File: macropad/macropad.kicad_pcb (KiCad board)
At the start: 2 copper layers, 77.5 x 61 mm, 45 parts, among them IC1 W25Q16JVUXIQ_TR, J1 Conn_01x03_Female, J2 USB_C_Receptacle, SW1 BOOT, SW2 RESET, U1 RP2040, U10 DRV5057A3, U11 DRV5057A3, U12 OLED_256x64_I2C, U2 DRV5057A3, U3 DRV5057A3, U4 DRV5057A3, U5 DRV5057A3, U6 CD74HC4067SM96E4, U7 DRV5057A3, U8 DRV5057A3, U9 NCP1117-3.3_SOT223, Y1 ABLS-12.000MHZ-B4-T

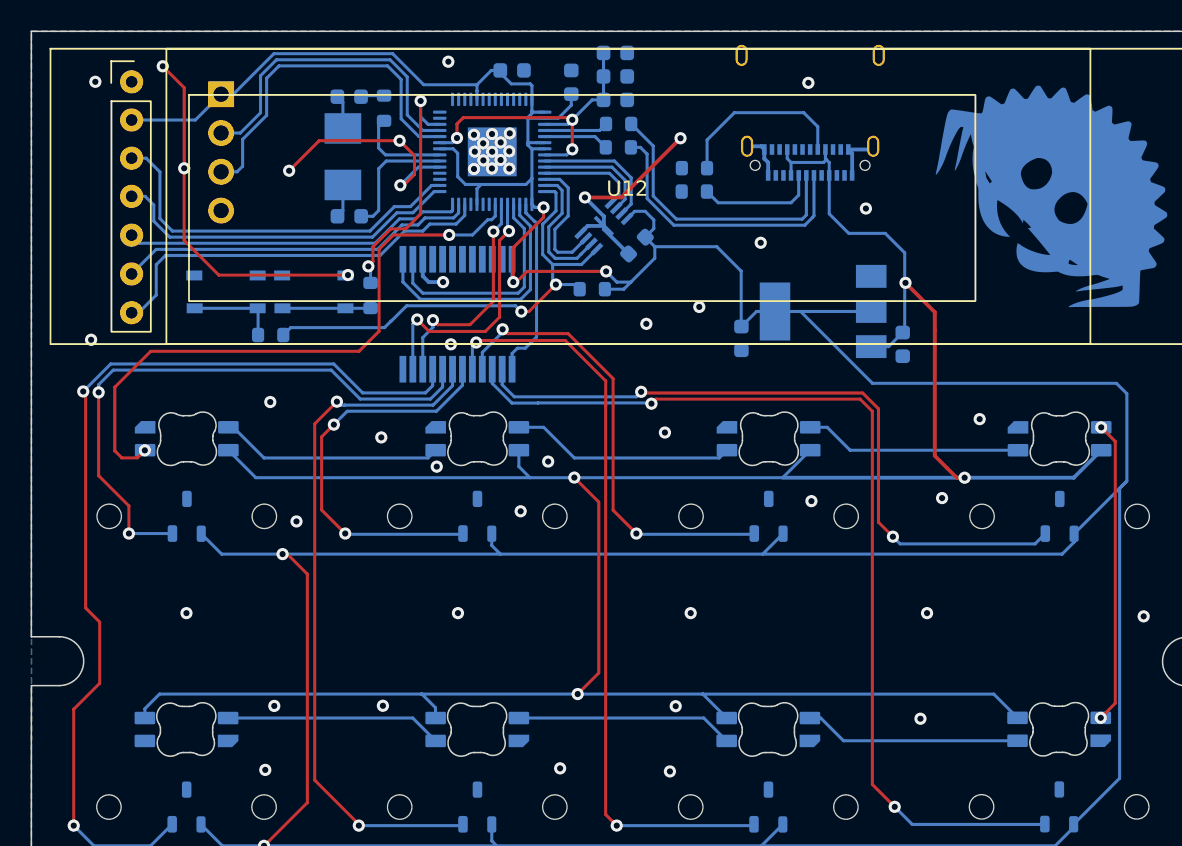
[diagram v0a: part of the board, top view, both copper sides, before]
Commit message: fix multiple issues with macropad pcb
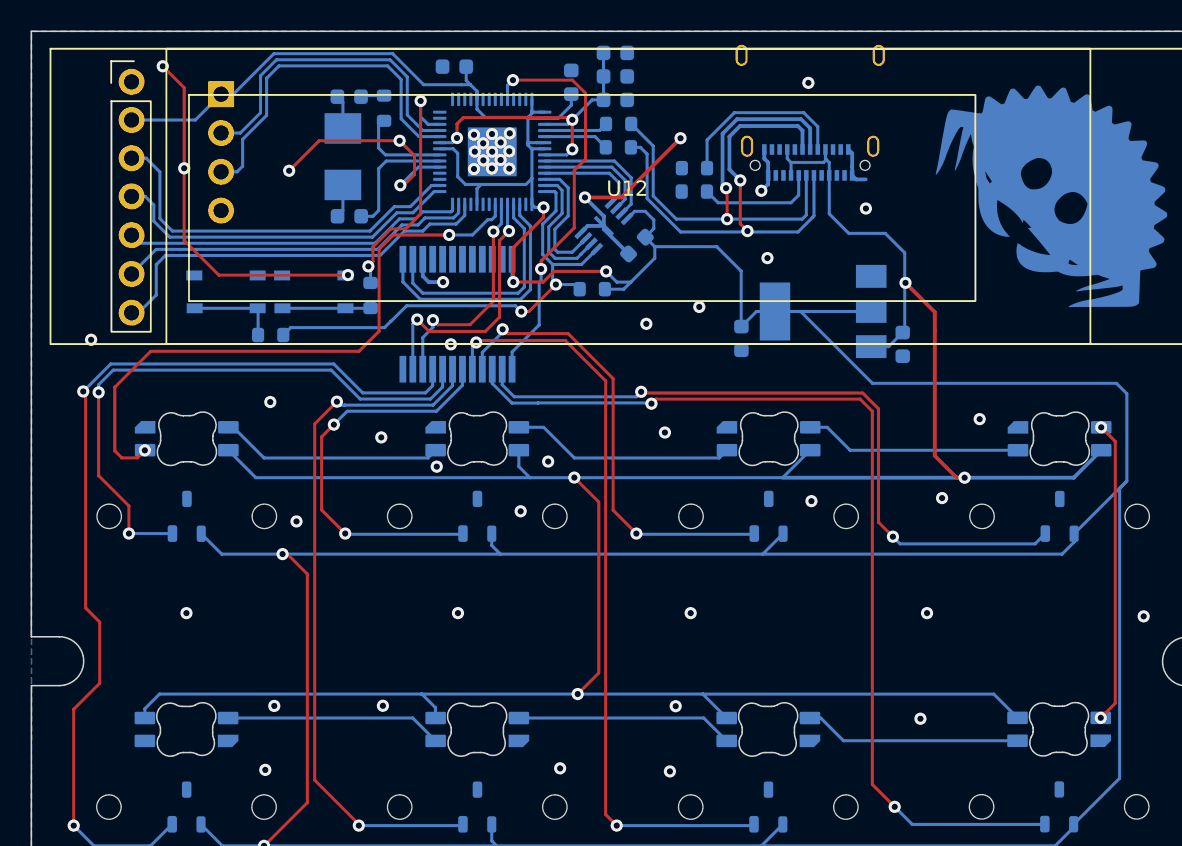
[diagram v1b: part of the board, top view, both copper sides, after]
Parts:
- LED2, LED4, LED6, LED8: footprint lib:LED_MX_SK6812MINI-R -> lib:LED_MX_SK6812MINI-R_FLIPPED
- U10, U11, U2, U3, U4, U5, U7, U8: value DRV5057A3 -> DRV5056A2; footprint lib:DRV5057A3_K -> lib:DRV505x
- Y1: value ABLS-12.000MHZ-B4-T -> ECS-120-8-30-JGN-TR
- moved LED1 5.08 mm to (131.9, 104.2), turned to 180 degrees
- moved LED2 5.08 mm to (131.8, 123.2), turned to 180 degrees
- moved LED3 5.08 mm to (150.9, 104.2), turned to 180 degrees
- moved LED4 5.08 mm to (150.9, 123.2), turned to 180 degrees
- moved LED5 5.08 mm to (170.0, 104.2), turned to 180 degrees
- moved LED6 5.08 mm to (169.9, 123.2), turned to 180 degrees
- moved LED7 5.08 mm to (189.0, 104.2), turned to 180 degrees
- moved LED8 5.08 mm to (189.0, 123.2), turned to 180 degrees
- moved C8 3.79 mm to (149.4, 74.8), turned to 180 degrees
- turned U10 to 180 degrees
- turned U11 to 180 degrees
- turned U2 to 180 degrees
- turned U3 to 180 degrees
- turned U4 to 180 degrees
- turned U5 to 180 degrees
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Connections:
- J2 pad A6: Net-(J2-PadA6) -> Net-(J2-D+-PadA6)
- J2 pad A7: Net-(J2-PadA7) -> Net-(J2-D--PadA7)
- J2 pad B6: unconnected-(J2-PadB6) -> Net-(J2-D+-PadA6)
- J2 pad B7: unconnected-(J2-PadB7) -> Net-(J2-D--PadA7)
- J2 pad S1: GND -> unconnected-(J2-SHIELD-PadS1)
- R4 pad 1: Net-(J2-PadA6) -> Net-(J2-D+-PadA6)
- R5 pad 1: Net-(J2-PadA7) -> Net-(J2-D--PadA7)
- U1 pad 2: /MUX1 COM -> unconnected-(U1-GPIO0-Pad2)
- U1 pad 38: unconnected-(U1-Pad38) -> /MUX1 COM
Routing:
- net Net-(J2-D--PadA7): track 0.00 -> 32.2 mm, vias 0 -> 2
- net Net-(J2-D+-PadA6): track 0.00 -> 32.2 mm, vias 0 -> 2
- net Net-(J2-PadA7): track 18.7 -> 0.00 mm
- net Net-(J2-PadA6): track 18.7 -> 0.00 mm
- net /MUX1 COM: track 12.1 -> 26.6 mm, vias 0 -> 2
- net GND: track 62.2 -> 61.5 mm, vias 58 -> 57

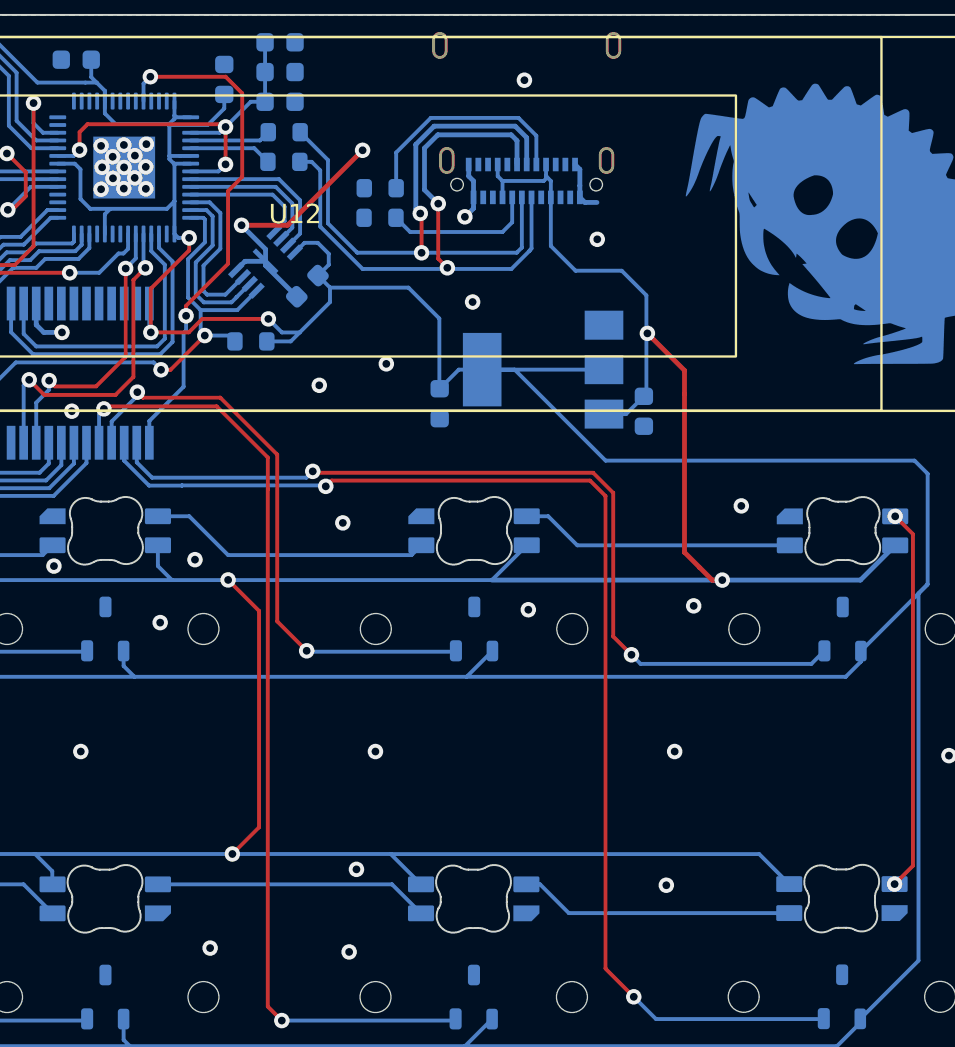
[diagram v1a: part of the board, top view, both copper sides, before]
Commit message: flip usb data lines to correct orientation
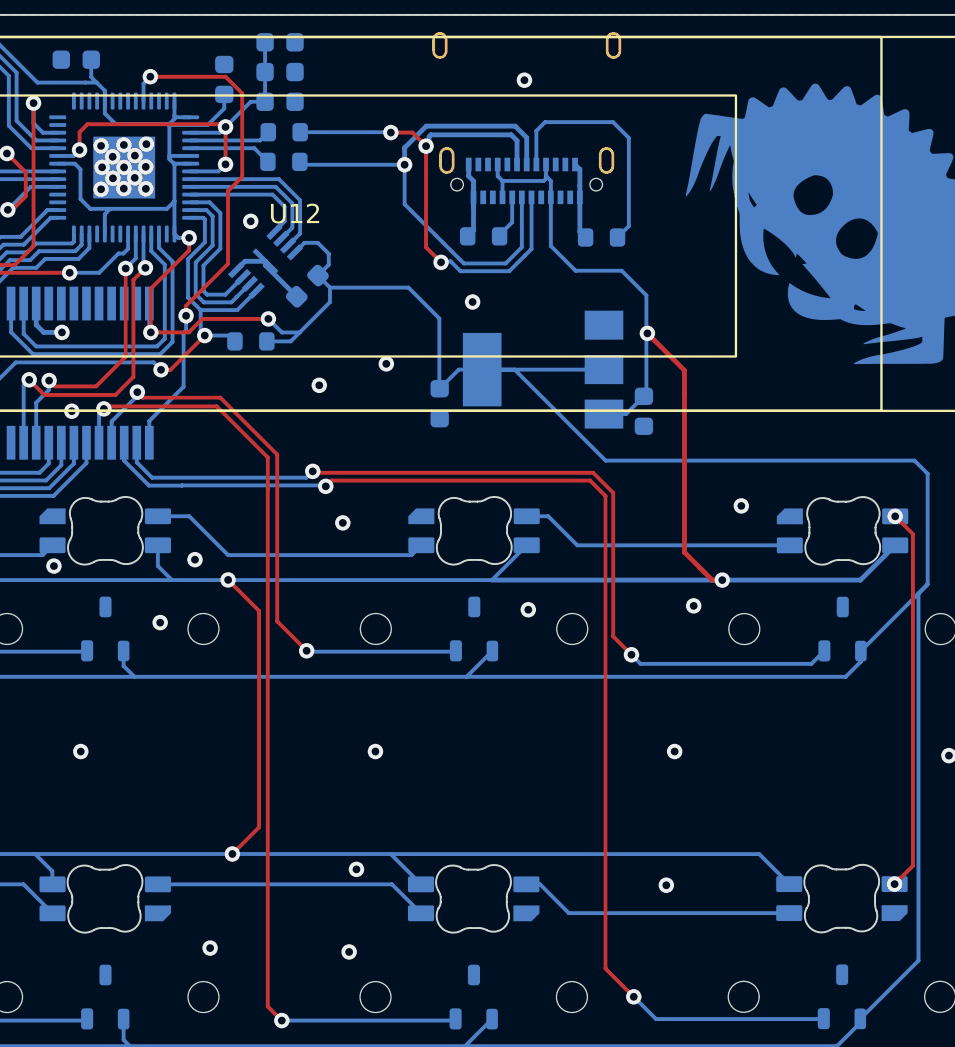
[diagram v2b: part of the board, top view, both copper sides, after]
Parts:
- moved R6 11.7 mm to (176.6, 84.0)
- moved R7 5.45 mm to (170.5, 83.9)
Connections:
- R4 pad 1: Net-(J2-D+-PadA6) -> Net-(J2-D--PadA7)
- R5 pad 1: Net-(J2-D--PadA7) -> Net-(J2-D+-PadA6)
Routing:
- net GND: track 61.5 -> 54.5 mm, vias 57 -> 54
- net Net-(J2-CC1): track 7.81 -> 2.28 mm
- net Net-(J2-D+-PadA6): track 32.2 -> 27.1 mm, vias 2 -> 1
- net Net-(J2-D--PadA7): track 32.2 -> 27.9 mm, vias 2 -> 3
- net Net-(J2-CC2): track 11.7 -> 12.4 mm

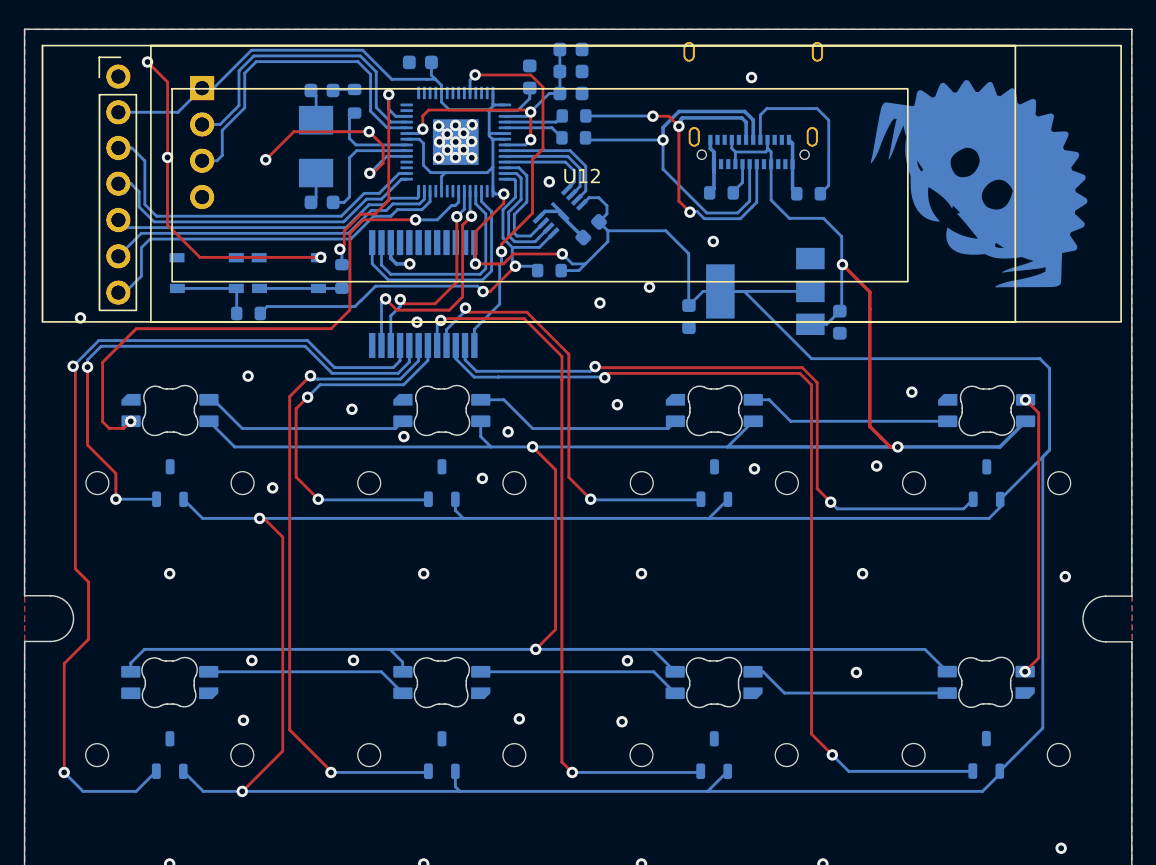
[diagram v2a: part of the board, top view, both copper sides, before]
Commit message: rework macropad usb data lines
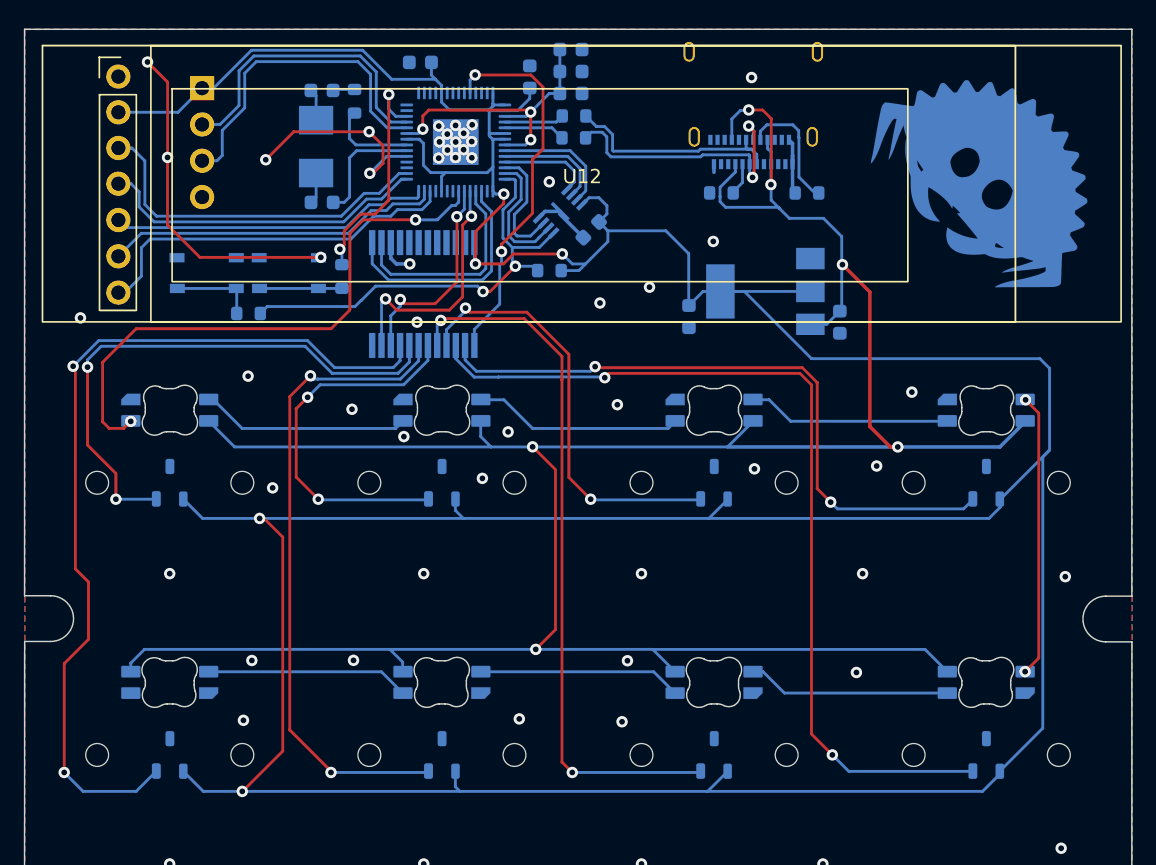
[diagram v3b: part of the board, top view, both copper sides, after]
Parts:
- moved R6 0.13 mm to (176.4, 83.9)
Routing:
- net +5V: track 178.6 -> 191.2 mm, vias 4 -> 6
- net Net-(J2-D--PadA7): track 27.9 -> 15.5 mm, vias 3 -> 0
- net Net-(J2-D+-PadA6): track 27.1 -> 19.6 mm, vias 1 -> 2
- net GND: track 54.5 -> 50.5 mm
- net Net-(J2-CC2): track 12.4 -> 8.82 mm

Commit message: whatever the fuck i all did
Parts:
- moved C2 68.8 mm to (82.9, 42.4)
- moved C3 68.8 mm to (82.9, 50.2)
- moved C4 68.8 mm to (97.4, 41.4)
- moved C6 68.8 mm to (119.1, 58.6)
- moved C8 68.8 mm to (89.8, 40.4)
- moved IC1 68.8 mm to (99.6, 50.9)
- moved J1 68.8 mm to (74.5, 42.2)
- moved J2 68.8 mm to (113.1, 42.5)
- moved LED3 68.8 mm to (91.3, 69.9)
- moved LED4 68.8 mm to (91.3, 88.9)
- moved LED7 68.8 mm to (129.4, 69.9)
- moved LED8 68.8 mm to (129.4, 88.9)
- moved R3 68.8 mm to (85.2, 43.1)
- moved R5 68.8 mm to (100.5, 45.7)
- moved R6 68.8 mm to (116.8, 49.6)
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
